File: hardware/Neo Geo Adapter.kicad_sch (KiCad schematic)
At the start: 25 parts, among them J101 AVR-UPDI-6, J102 Playstation, J103 Saturn, J104 NEO_GEO, SW101 AF_A, SW102 AF_B, SW103 AF_C, SW104 AF_D, SW105 AUTO, SW106 MODE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

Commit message: Fixed PDI header gender, KiCad 8
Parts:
- J101: footprint Connector_PinSocket_1.27mm:PinSocket_2x03_P1.27mm_Vertical_SMD -> Connector_PinHeader_1.27mm:PinHeader_2x03_P1.27mm_Vertical_SMD

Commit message: Added BOM
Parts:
- H101, H102, H103, H104, JP101, TP101: now left out of the parts list
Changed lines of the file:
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@@
 		(unit 1)
 		(exclude_from_sim no)
-		(in_bom yes)
+		(in_bom no)
 		(on_board yes)
 		(dnp no)
@@
 		(unit 1)
 		(exclude_from_sim no)
-		(in_bom yes)
+		(in_bom no)
 		(on_board yes)
 		(dnp no)
@@
 		(unit 1)
 		(exclude_from_sim no)
-		(in_bom yes)
+		(in_bom no)
 		(on_board yes)
 		(dnp no)
@@
 		(unit 1)
 		(exclude_from_sim no)
-		(in_bom yes)
+		(in_bom no)
 		(on_board yes)
 		(dnp no)
@@
 			)
 		)
+		(property "DNP" ""
+			(at 139.7 176.53 0)
+			(effects
+				(font
+					(size 1.27 1.27)
+				)
+				(hide yes)
+			)
+		)
 		(instances
 			(project "Neo Geo Adapter"
@@
 		(unit 1)
 		(exclude_from_sim no)
-		(in_bom yes)
+		(in_bom no)
 		(on_board yes)
 		(dnp no)
@@
 			)
 		)
+		(property "DNP" ""
+			(at 139.7 186.69 0)
+			(effects
+				(font
+					(size 1.27 1.27)
+				)
+				(hide yes)
+			)
+		)
 		(instances
 			(project "Neo Geo Adapter"
@@
 		(unit 1)
 		(exclude_from_sim no)
-		(in_bom yes)
+		(in_bom no)
 		(on_board yes)
 		(dnp no)
@@
 			(at 139.7 181.61 0)
 			(effects
+				(font
+					(size 1.27 1.27)
+				)
+				(hide yes)
+			)
+		)
+		(property "DNP" ""
+			(at 139.7 181.61 0)
+			(effects

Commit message: 15 pin connector part and 3D model
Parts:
- J104: MPN (none) -> Amphenol L77SDA15SA4CH4F
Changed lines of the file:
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@@
+			)
+		)
+		(property "MPN" "Amphenol L77SDA15SA4CH4F"
+			(at 189.23 38.1 0)
+			(effects
+				(font
+					(size 1.27 1.27)
+				)
+				(hide yes)
 			)
 		)

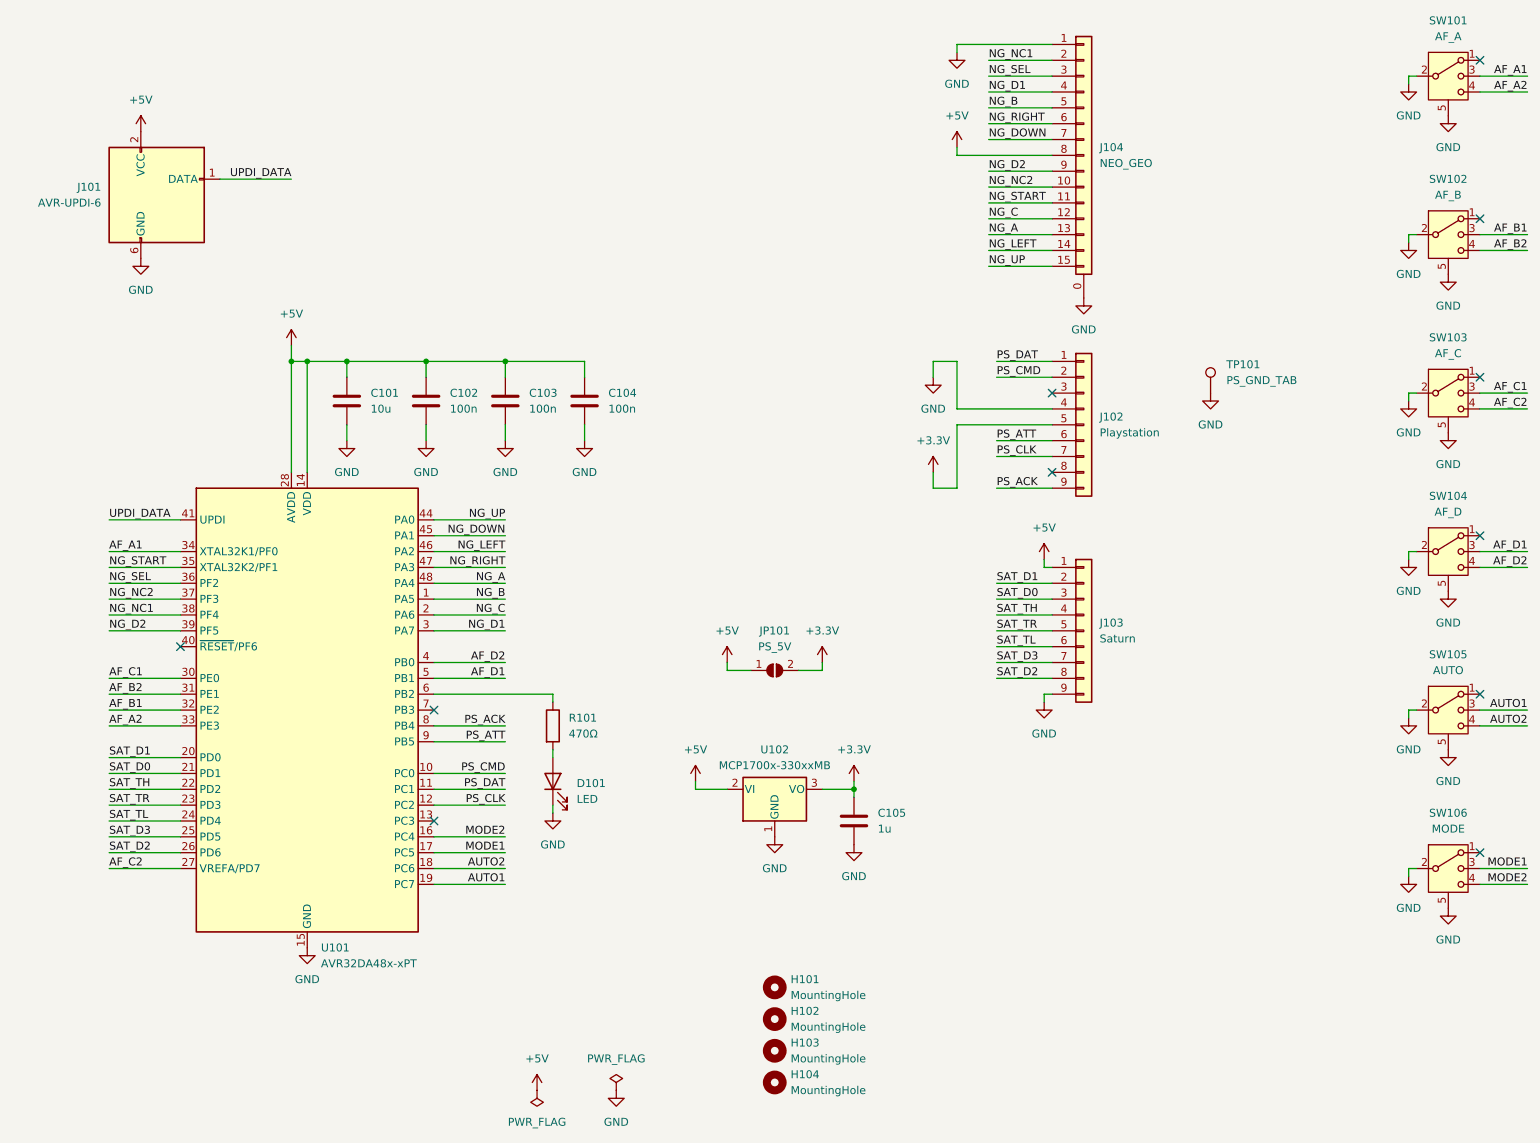
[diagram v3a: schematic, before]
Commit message: Playstation 3V3 power and signalling
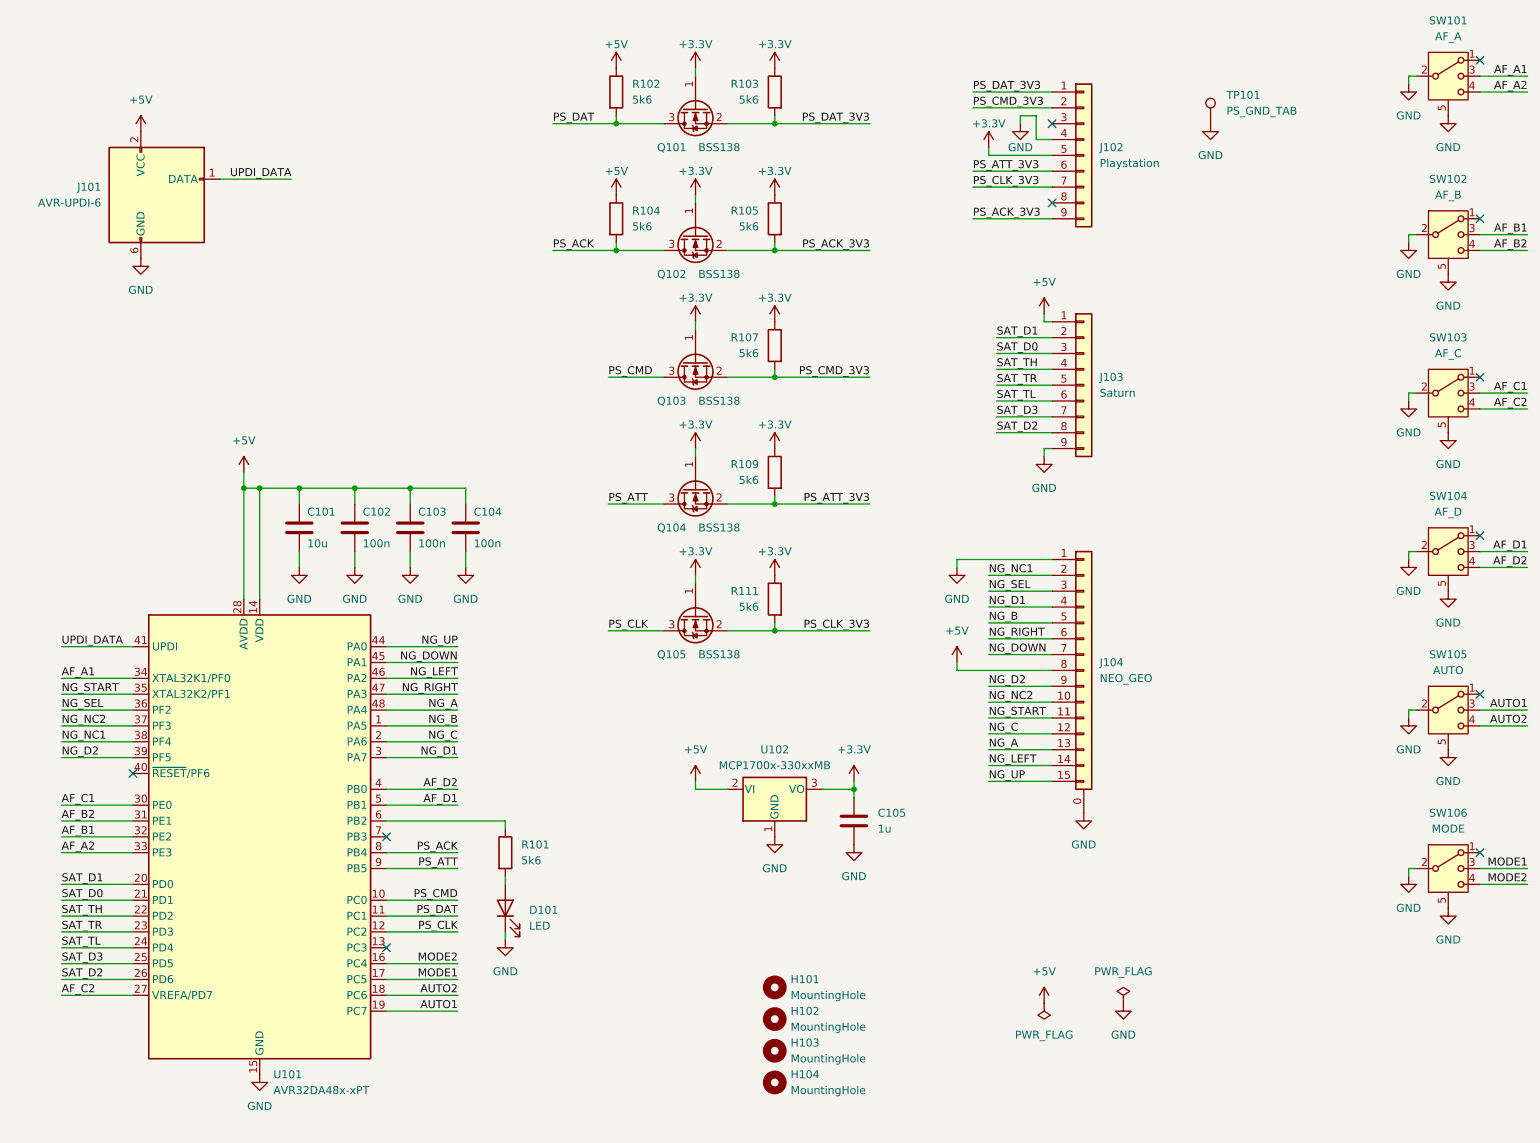
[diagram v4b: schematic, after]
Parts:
- removed JP101: PS_5V, Jumper:SolderJumper-2_P1.3mm_Open_RoundedPad1.0x1.5mm, symbol Jumper:SolderJumper_2_Open
- added Q101, Q102, Q103, Q104, Q105: BSS138, Package_TO_SOT_SMD:SOT-23, symbol Transistor_FET:BSS138
- added R102, R103, R104, R105, R107, R109, R111: 5k6, Resistor_SMD:R_0805_2012Metric_Pad1.20x1.40mm_HandSolder, symbol Device:R
- R101: value 470Ω -> 5k6
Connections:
- net +3.3V: now also Q101.1 (G), Q102.1 (G), Q103.1 (G), Q104.1 (G), Q105.1 (G), R103.1, R105.1, R107.1, R109.1, R111.1
- net +5V: now also R102.1, R104.1
- net PS_ACK: now also Q102.3 (D), R104.2; no longer J102.9 (Pin_9)
- net PS_ATT: now also Q104.3 (D); no longer J102.6 (Pin_6)
- net PS_CLK: now also Q105.3 (D); no longer J102.7 (Pin_7)
- net PS_CMD: now also Q103.3 (D); no longer J102.2 (Pin_2)
- net PS_DAT: now also Q101.3 (D), R102.2; no longer J102.1 (Pin_1)
- new net PS_ACK_3V3: J102.9 (Pin_9), Q102.2 (S), R105.2
- new net PS_ATT_3V3: J102.6 (Pin_6), Q104.2 (S), R109.2
- new net PS_CLK_3V3: J102.7 (Pin_7), Q105.2 (S), R111.2
- new net PS_CMD_3V3: J102.2 (Pin_2), Q103.2 (S), R107.2
- new net PS_DAT_3V3: J102.1 (Pin_1), Q101.2 (S), R103.2
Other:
- moved on the sheet: C101, C102, C103, C104, D101, J102, J103, J104, R101, TP101, U101

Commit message: Rev 2 RTM
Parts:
- removed Q101, Q102: BSS138, Package_TO_SOT_SMD:SOT-23, symbol Transistor_FET:BSS138
- removed R102, R104: 5k6, Resistor_SMD:R_0805_2012Metric_Pad1.20x1.40mm_HandSolder, symbol Device:R
- U101: value AVR32DA48x-xPT -> AVR32EA48x-xPT
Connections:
- net PS_ACK_3V3 is gone; now on net PS_ACK: J102.9 (Pin_9), R105.2
- net PS_DAT_3V3 is gone; now on net PS_DAT: J102.1 (Pin_1), R103.2
